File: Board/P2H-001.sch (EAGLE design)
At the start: 27 parts, among them IC1 LTC485N, IC2 74LS07N, IC3 74LS157N, IC4 LTC485N, IC5 TLC5941NT

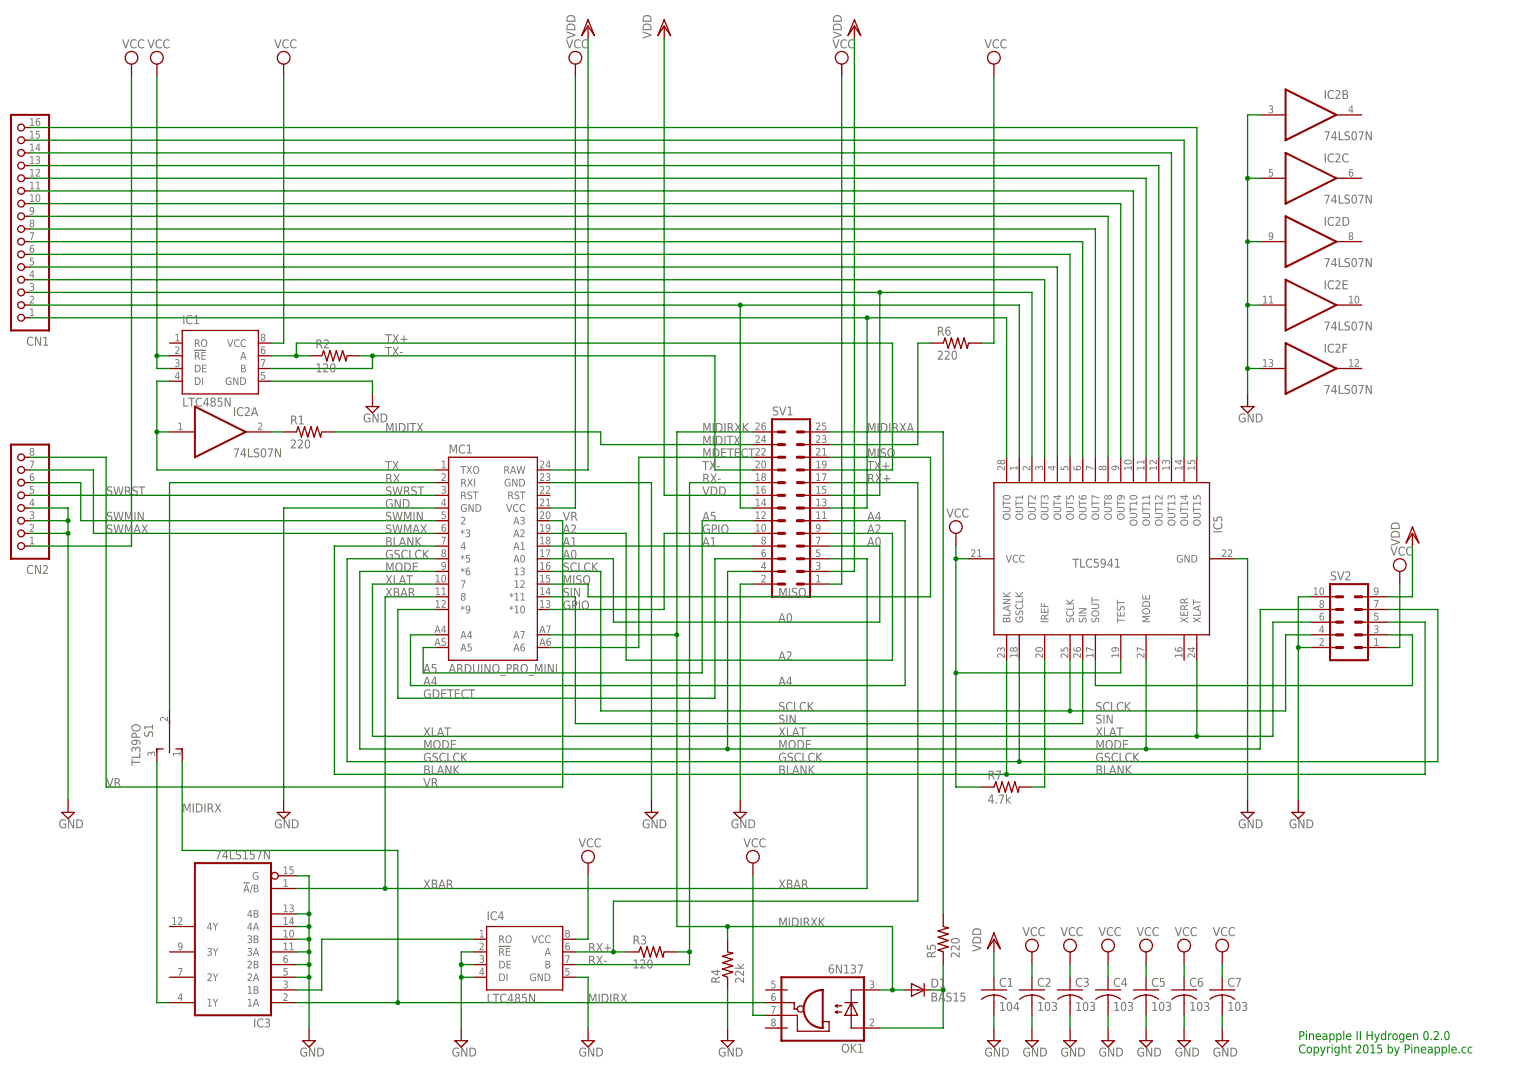
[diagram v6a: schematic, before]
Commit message: Layout change.
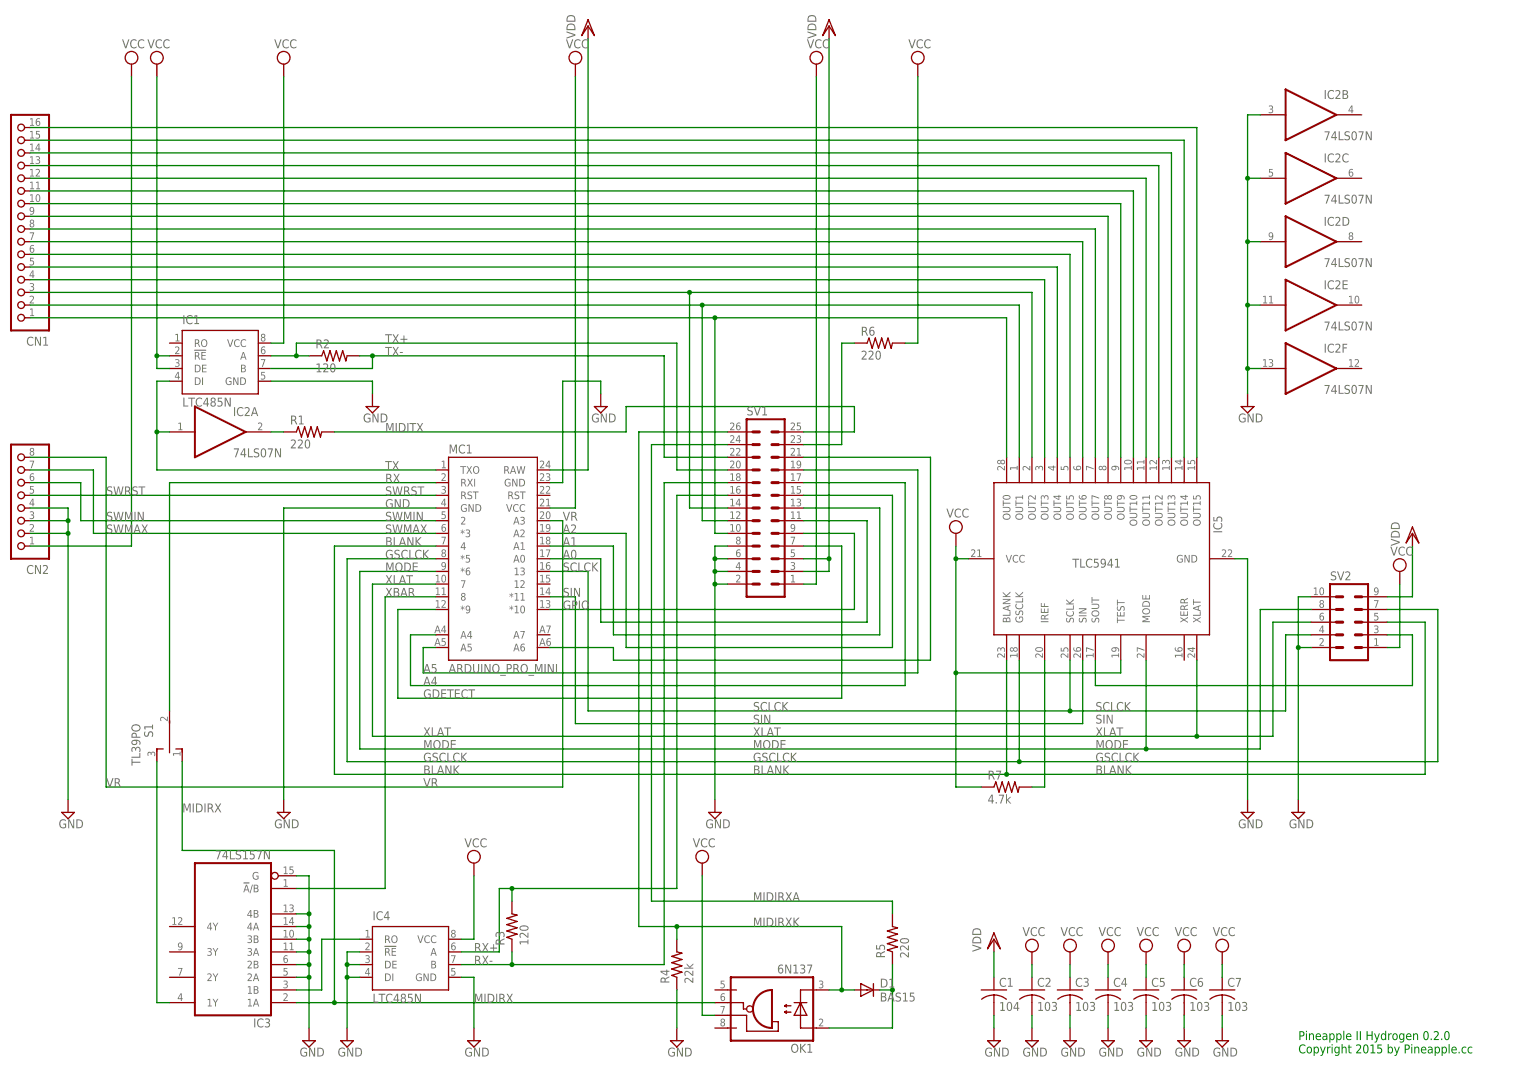
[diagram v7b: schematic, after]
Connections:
- removed net MDETECT: MC1.A6, SV1.22
- removed net MISO: MC1.12, SV1.21
- new net N$4: MC1.A6, SV1.21
- net A0: now also SV1.11; no longer SV1.7
- net A1: now also SV1.13; no longer SV1.8
- net A2: now also SV1.15; no longer SV1.9
- net A4: now also SV1.17; no longer SV1.11
- net A5: now also SV1.19; no longer SV1.12
- net GDETECT: now also SV1.7; no longer SV1.6
- net GND: now also SV1.4, SV1.6, SV1.8
- net GPIO: now also SV1.9; no longer SV1.10
- net LEDA: now also SV1.10; no longer SV1.13
- net MIDIRXA: now also SV1.24; no longer SV1.25
- net MIDIRXK: no longer MC1.A7
- net MIDITX: now also SV1.25; no longer SV1.24
- net MODE: no longer SV1.4
- net N$12: now also SV1.12; no longer SV1.14
- net N$14: now also SV1.14; no longer SV1.15
- net RX+: now also R3.2, SV1.16; no longer R3.1, SV1.17
- net RX-: now also R3.1; no longer R3.2
- net TX+: now also SV1.20; no longer SV1.19
- net TX-: now also SV1.22; no longer SV1.20
- net VDD: now also SV1.5; no longer SV1.16
- net XBAR: no longer SV1.5
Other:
- moved on the sheet: D1, IC4, OK1, R3, R4, R5, R6, SV1

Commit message: Fixed panel LED layout.
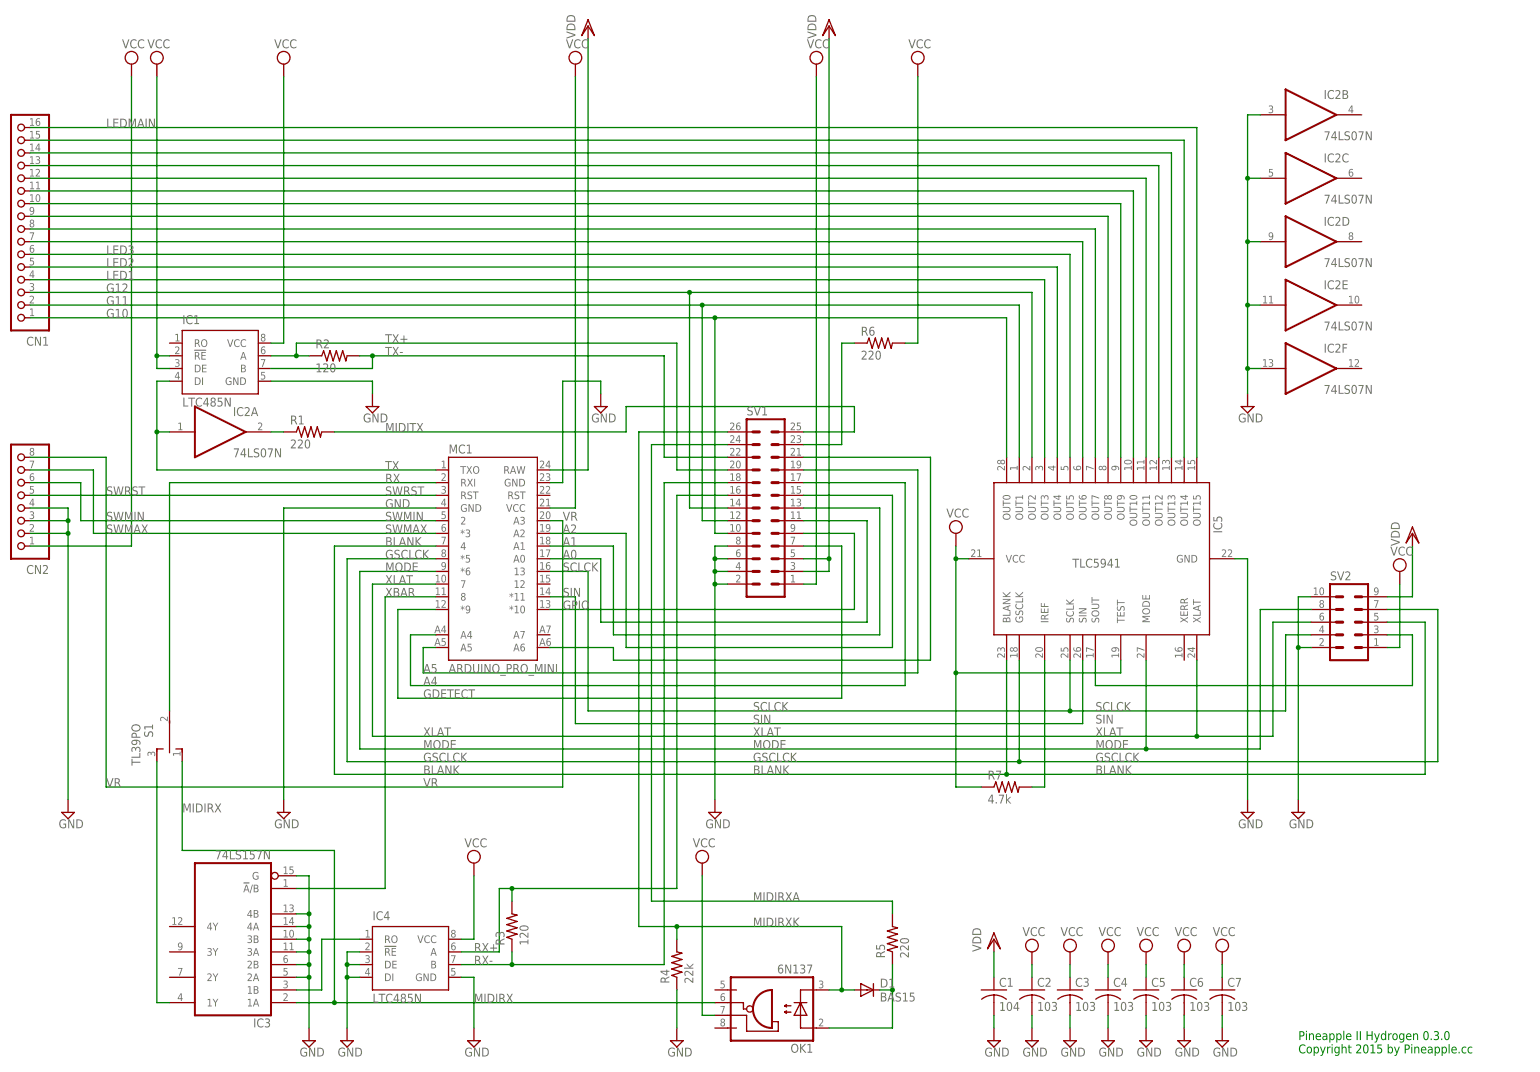
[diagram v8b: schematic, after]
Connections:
- net LED2B renamed LED3
- net LED2G renamed LED2
- net LEDA renamed G10
- net N$12 renamed G11
- net N$14 renamed G12
- net N$25 renamed LEDMAIN
- net N$9 renamed LED1
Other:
- note added: "Pineapple II Hydrogen 0.3.0 Copyright 2015 by Pineapple.cc"
- note removed: "Pineapple II Hydrogen 0.2.0 Copyright 2015 by Pineapple.cc"
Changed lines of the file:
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@@
 <setting verticaltext="up"/>
 </settings>
-<grid distance="0.1" unitdist="inch" unit="inch" style="lines" multiple="1" display="yes" altdistance="0.01" altunitdist="inch" altunit="inch"/>
+<grid distance="0.1" unitdist="inch" unit="inch" style="lines" multiple="1" display="no" altdistance="0.01" altunitdist="inch" altunit="inch"/>
 <layers>
 <layer number="1" name="Top" color="4" fill="1" visible="no" active="no"/>
@@
 <sheet>
 <plain>
-<text x="259.08" y="-71.12" size="1.778" layer="91">Pineapple II Hydrogen 0.2.0
+<text x="259.08" y="-71.12" size="1.778" layer="91">Pineapple II Hydrogen 0.3.0
 Copyright 2015 by Pineapple.cc</text>
 </plain>
@@
 </segment>
 </net>
-<net name="LED2G" class="0">
+<net name="LED2" class="0">
 <segment>
 <pinref part="IC5" gate="G$1" pin="OUT4"/>
@@
 <wire x1="5.08" y1="86.36" x2="210.82" y2="86.36" width="0.1524" layer="91"/>
 <pinref part="CN1" gate="G$1" pin="5"/>
-</segment>
-</net>
-<net name="LED2B" class="0">
+<label x="20.32" y="86.36" size="1.778" layer="95"/>
+</segment>
+</net>
+<net name="LED3" class="0">
 <segment>
 <pinref part="IC5" gate="G$1" pin="OUT5"/>
@@
 <wire x1="5.08" y1="88.9" x2="213.36" y2="88.9" width="0.1524" layer="91"/>
 <pinref part="CN1" gate="G$1" pin="6"/>
+<label x="20.32" y="88.9" size="1.778" layer="95"/>
 </segment>
 </net>
@@
 </segment>
 </net>
-<net name="LEDA" class="0">
+<net name="G10" class="0">
 <segment>
 <pinref part="IC5" gate="G$1" pin="OUT0"/>
@@
 <wire x1="142.24" y1="33.02" x2="142.24" y2="76.2" width="0.1524" layer="91"/>
 <junction x="142.24" y="76.2"/>
-</segment>
-</net>
-<net name="N$12" class="0">
+<label x="20.32" y="76.2" size="1.778" layer="95"/>
+</segment>
+</net>
+<net name="G11" class="0">
 <segment>
 <pinref part="IC5" gate="G$1" pin="OUT1"/>
@@
 <wire x1="139.7" y1="35.56" x2="139.7" y2="78.74" width="0.1524" layer="91"/>
 <junction x="139.7" y="78.74"/>
-</segment>
-</net>
-<net name="N$14" class="0">
+<label x="20.32" y="78.74" size="1.778" layer="95"/>
+</segment>
+</net>
+<net name="G12" class="0">
 <segment>
 <pinref part="IC5" gate="G$1" pin="OUT2"/>
@@
 <wire x1="137.16" y1="38.1" x2="137.16" y2="81.28" width="0.1524" layer="91"/>
 <junction x="137.16" y="81.28"/>
+<label x="20.32" y="81.28" size="1.778" layer="95"/>
 </segment>
 </net>
@@
 </segment>
 </net>
-<net name="N$25" class="0">
+<net name="LEDMAIN" class="0">
 <segment>
 <pinref part="IC5" gate="G$1" pin="OUT15"/>
@@
 <wire x1="5.08" y1="114.3" x2="238.76" y2="114.3" width="0.1524" layer="91"/>
 <pinref part="CN1" gate="G$1" pin="16"/>
+<label x="20.32" y="114.3" size="1.778" layer="95"/>
 </segment>
 </net>
@@
 </segment>
 </net>
-<net name="N$9" class="0">
+<net name="LED1" class="0">
 <segment>
 <pinref part="IC5" gate="G$1" pin="OUT3"/>
@@
 <wire x1="208.28" y1="83.82" x2="5.08" y2="83.82" width="0.1524" layer="91"/>
 <pinref part="CN1" gate="G$1" pin="4"/>
-</segment>
-</net>
+<label x="20.32" y="83.82" size="1.778" layer="95"/>
+</segment>
+</net>
